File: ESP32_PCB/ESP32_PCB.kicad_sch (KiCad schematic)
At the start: 27 parts, among them J1 USB_C_Receptacle, J2 ESC 1, J3 ESC 2, J4 EN & Boot, J5 LED, U2 H3LIS331DL, U3 AP2112K-3.3, U5 ESP32-S3-MINI-1U

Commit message: rerouting
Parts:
- removed C3: 10uF, Capacitor_SMD:C_0805_2012Metric, symbol Device:C_Small_US
- removed C4: .1uF, Capacitor_SMD:C_0603_1608Metric, symbol Device:C_Small_US

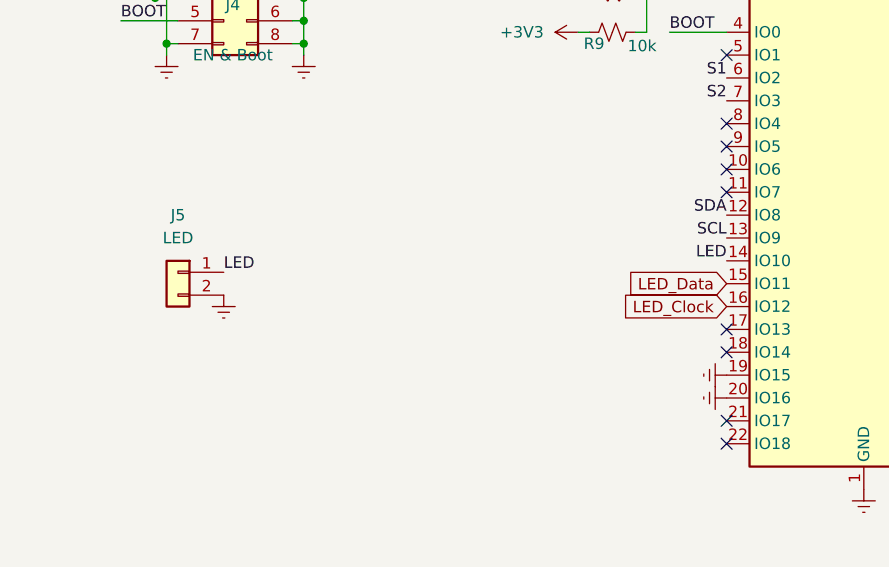
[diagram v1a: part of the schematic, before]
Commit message: Add LED strip
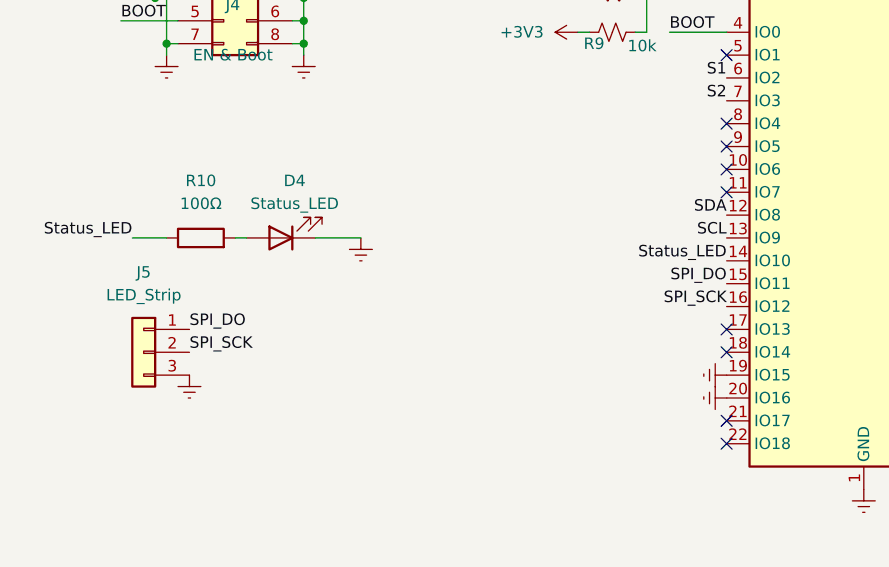
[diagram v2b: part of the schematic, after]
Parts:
- removed J5: LED, ESC_Connectors:2_Pin, symbol Connector_Generic:Conn_01x02
- added D4: Status_LED, LED_SMD:LED_0603_1608Metric, symbol Device:LED
- added J5: LED_Strip, ESC_Connectors:LED_Strip, symbol Connector_Generic:Conn_01x03
- added R10: 100Ω, Resistor_SMD:R_0603_1608Metric, symbol Device:R
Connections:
- net GNDREF: now also D4.1 (K), J5.3 (Pin_3)
- net LED renamed Status_LED
- net Status_LED: now also R10.1
- net LED_Clock renamed SPI_SCK
- net SPI_SCK: now also J5.2 (Pin_2)
- net LED_Data renamed SPI_DO
- net SPI_DO: now also J5.1 (Pin_1)
- new net: D4.2 (A), R10.2

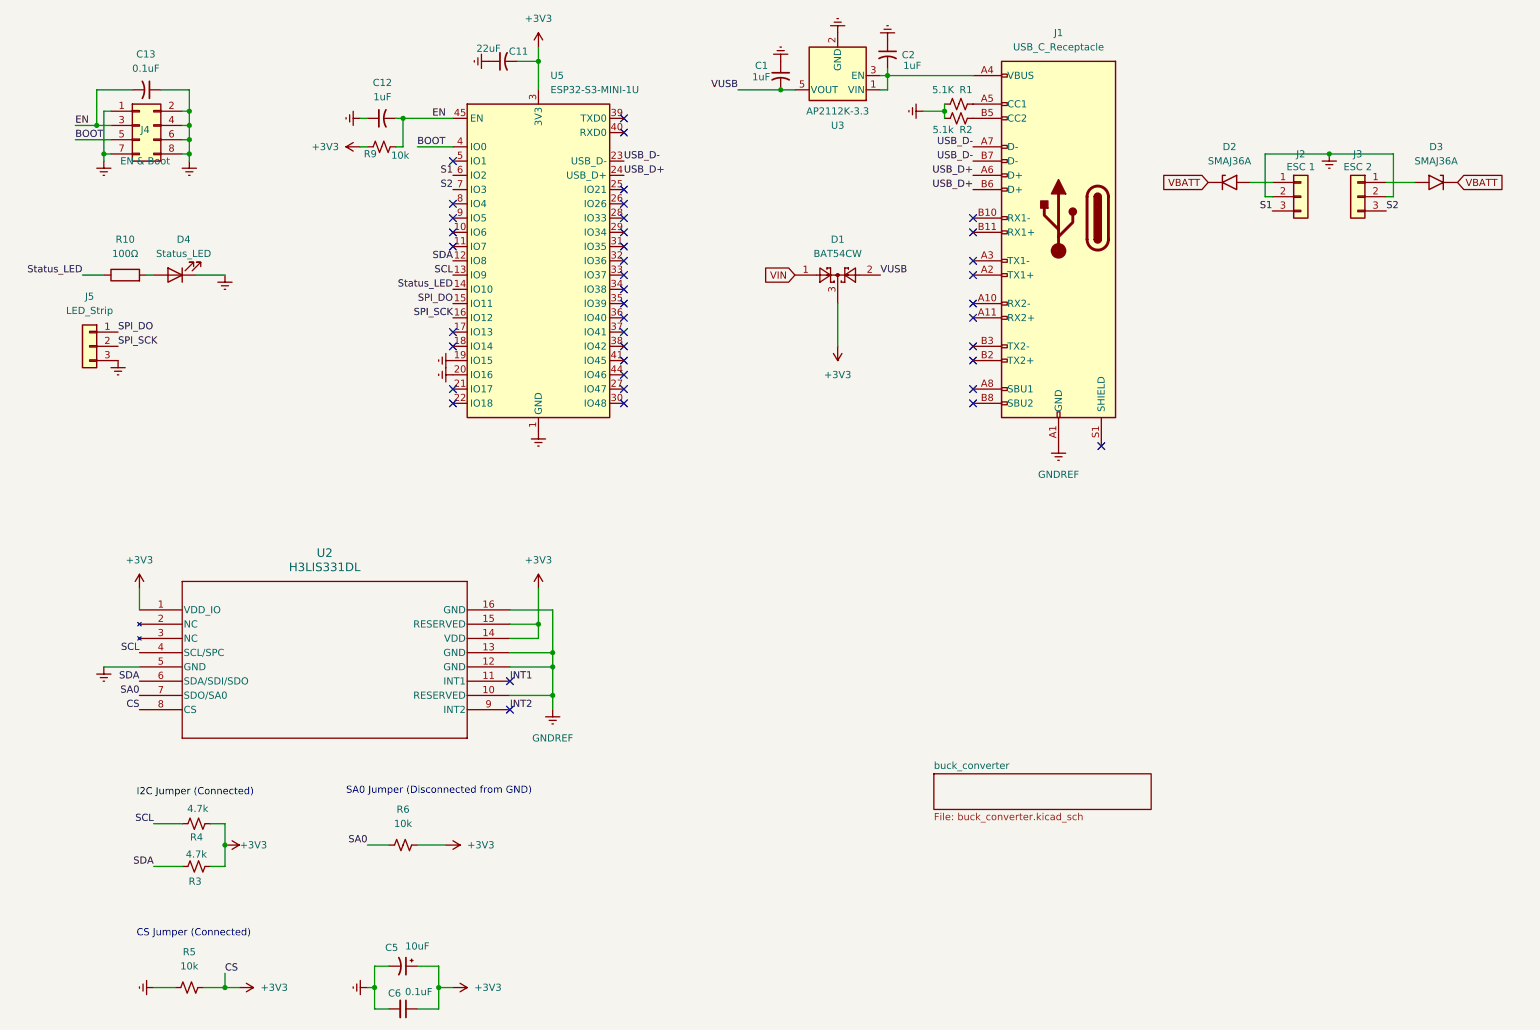
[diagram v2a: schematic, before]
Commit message: Add LED to indicate the power
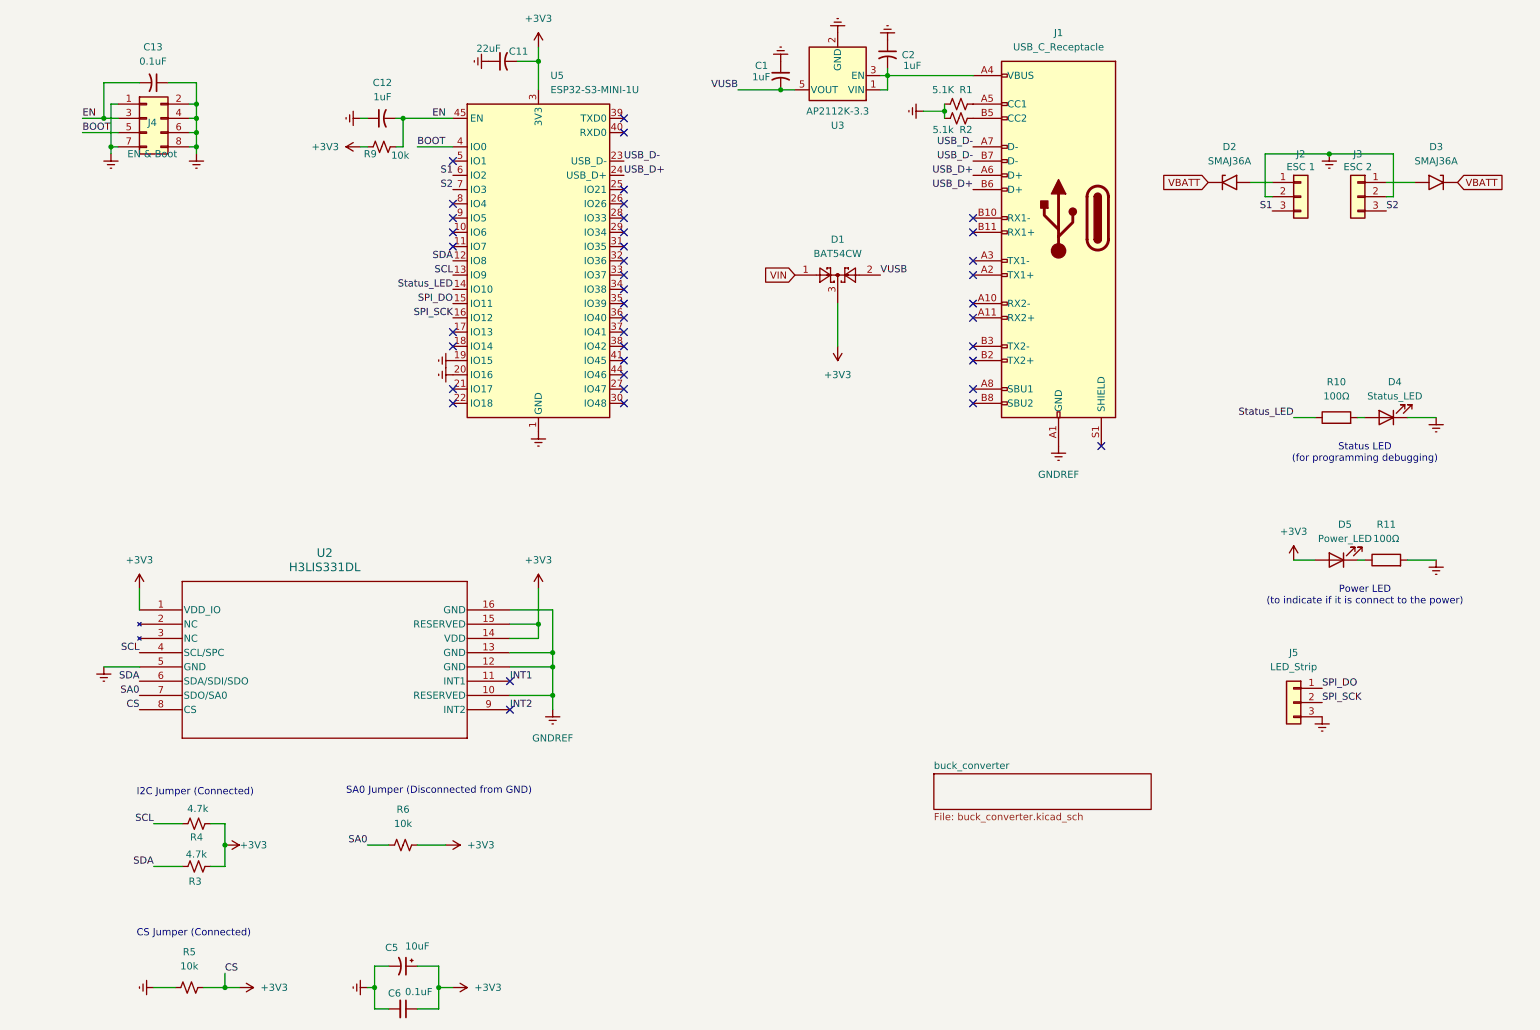
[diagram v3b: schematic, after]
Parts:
- added D5: Power_LED, LED_SMD:LED_0603_1608Metric, symbol Device:LED
- added R11: 100Ω, Resistor_SMD:R_0603_1608Metric, symbol Device:R
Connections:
- net +3V3: now also D5.2 (A)
- net GNDREF: now also R11.2
- new net: D5.1 (K), R11.1
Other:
- note added: "Power LED (to indicate if it is connect to the power)"
- note added: "Status LED (for programming debugging)"
- moved on the sheet: C13, D4, J4, J5, R10

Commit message: add lcsc pn
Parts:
- C1, C12, C13, C2, C6: LCSC PN (none) -> C15849
- C11: LCSC PN (none) -> C86295
- C5: footprint Capacitor_Tantalum_SMD:CP_EIA-1608-08_AVX-J -> Capacitor_Tantalum_SMD:CP_EIA-3216-18_Kemet-A; LCSC PN (none) -> C7171
- D1: LCSC PN (none) -> C192144
- D2, D3: LCSC PN (none) -> C148232
- D4: LCSC PN (none) -> C19273151
- D5: LCSC PN (none) -> C19171390
- J1: LCSC PN (none) -> C134092
- J4: LCSC PN (none) -> C32713277
- R1, R2: LCSC PN (none) -> C2907044
- R10, R11: LCSC PN (none) -> C105588
- R3, R4: LCSC PN (none) -> C99782
- R5, R6, R9: LCSC PN (none) -> C98220
- U2: LCSC PN (none) -> C2655074
- U3: LCSC PN (none) -> C23380830
- U5: LCSC PN (none) -> C2980299

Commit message: Fix LCSC and PCB
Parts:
- removed C12: 1uF, Capacitor_SMD:C_0201_0603Metric, symbol Device:C_Small_US
- added C4: 1uF, Capacitor_SMD:C_0603_1608Metric, symbol Device:C_Small
- added C7: 10pF, Capacitor_SMD:C_0603_1608Metric, symbol Device:C_Small
- added R12: 10k, Resistor_SMD:R_0603_1608Metric, symbol Device:R_Small_US
- C13: value 0.1uF -> 100nF; footprint Capacitor_SMD:C_0201_0603Metric -> Capacitor_SMD:C_0603_1608Metric; LCSC PN C15849 -> C14663
- C6: value 0.1uF -> 100nF; LCSC PN C15849 -> C14663
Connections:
- net +3V3: now also R12.2
- net BOOT: now also C7.1, R12.1
- net EN: now also C13.1, C4.1; no longer C13.2
- net GNDREF: now also C13.2, C4.2, C7.2; no longer C13.1
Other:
- moved on the sheet: C13, R9

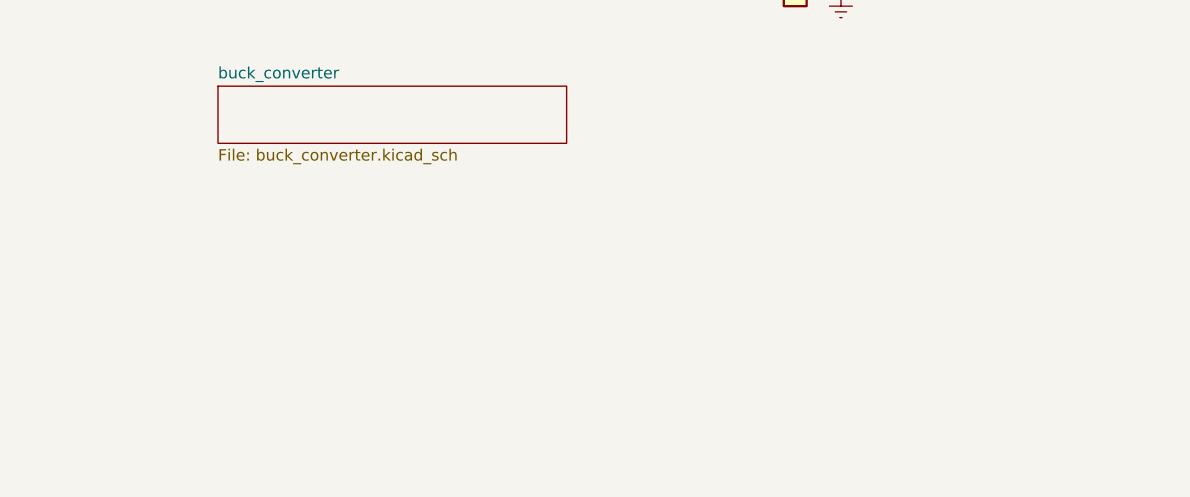
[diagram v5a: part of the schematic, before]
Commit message: add esp32s3 cnofig
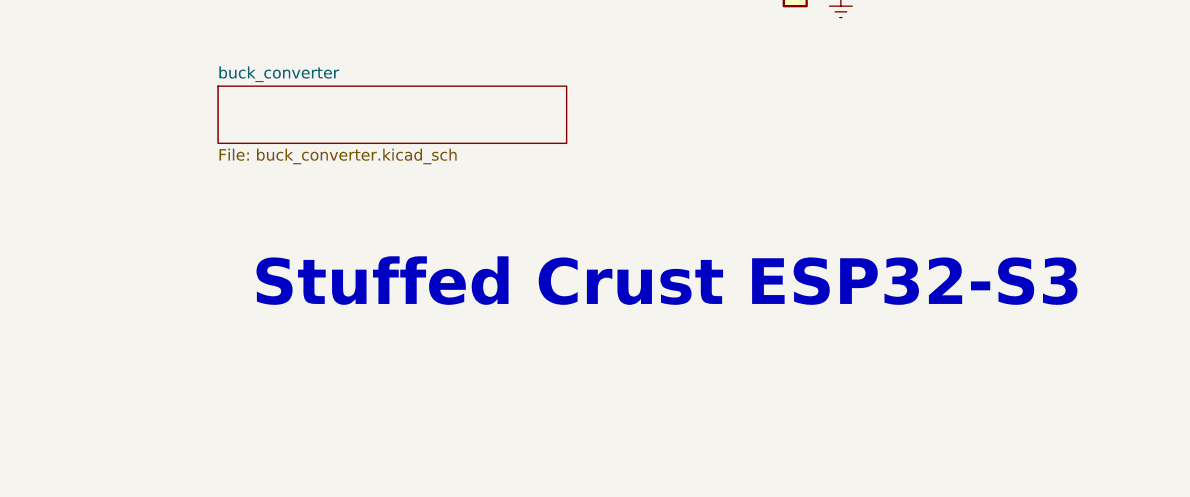
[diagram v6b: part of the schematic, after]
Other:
- note added: "Stuffed Crust ESP32-S3"
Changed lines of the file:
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@@
+		)
+	)
+	(text "Stuffed Crust ESP32-S3"
+		(exclude_from_sim no)
+		(at 227.076 174.498 0)
+		(effects
+			(font
+				(size 5.08 5.08)
+				(thickness 1.016)
+				(bold yes)
+			)
 		)
 	)
